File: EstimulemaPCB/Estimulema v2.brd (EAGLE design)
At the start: 151 x 162 mm, 159 parts, among them IC3 74AC14N, IC4 ISO7240S, J1 JUMPERS12MM, J2 J15MM, J3 J_7MM, J4 JUMPERS5MM, J5 JUMPERS7MM, J6 J7MM, K2 HC-06, Q17 TIP48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

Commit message: last version pcb file
ultima version pcb
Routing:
- net GPIO5: track 219.2 -> 222.0 mm
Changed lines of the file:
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@@
 <drawing>
 <settings>
-<setting alwaysvectorfont="yes"/>
+<setting alwaysvectorfont="no"/>
 <setting verticaltext="up"/>
 </settings>
@@
 </layers>
 <board>
-<fusionsync huburn="a.cGVyc29uYWw6dWUyOGM0MjA1" projecturn="a.cGVyc29uYWw6dWUyOGM0MjA1IzIwMTcxMjI2MTA5OTE4NzUx" f3durn="urn:adsk.wipprod:dm.lineage:a3TV6h6ST9ayQOR__9NI6g" pcbguid="653ef68f-6985-4a81-9d55-14a2d5d2a77c" lastpulledtime="" lastsyncedchangeguid="1821962e-2547-75dc-39ca-bfed1a03af76"/>
+<fusionsync huburn="a.cGVyc29uYWw6dWUyOGM0MjA1" projecturn="a.cGVyc29uYWw6dWUyOGM0MjA1IzIwMTcxMjI2MTA5OTE4NzUx" f3durn="urn:adsk.wipprod:dm.lineage:a3TV6h6ST9ayQOR__9NI6g" pcbguid="653ef68f-6985-4a81-9d55-14a2d5d2a77c" lastpulledtime="" lastsyncedchangeguid="752f2832-0191-109f-3336-40c44a7aafc6"/>
 <plain>
 <wire x1="1.016" y1="50" x2="152" y2="50" width="0" layer="20"/>
@@
 <wire x1="55.118" y1="196.596" x2="59.69" y2="196.596" width="0.3556" layer="16"/>
 <via x="59.69" y="196.596" extent="1-16" drill="0.9" diameter="2" shape="square"/>
-<wire x1="59.69" y1="196.596" x2="62.484" y2="196.596" width="0.3556" layer="1"/>
+<wire x1="62.484" y1="196.596" x2="59.69" y2="196.596" width="0.3556" layer="1"/>
 <via x="91.186" y="202.692" extent="1-16" drill="0.9" diameter="2" shape="square"/>
 <wire x1="91.186" y1="202.692" x2="100.584" y2="202.692" width="0.3556" layer="16"/>
@@
 <wire x1="124.5362" y1="90.0938" x2="122.936" y2="91.694" width="0.3556" layer="16"/>
 <wire x1="122.936" y1="106.934" x2="122.936" y2="91.694" width="0.3556" layer="16"/>
-<wire x1="62.484" y1="196.596" x2="68.58" y2="202.692" width="0.3556" layer="1"/>
-<wire x1="68.58" y1="202.692" x2="91.186" y2="202.692" width="0.3556" layer="1"/>
 <wire x1="100.584" y1="202.692" x2="101.092" y2="203.2" width="0.3556" layer="1"/>
 <wire x1="124.968" y1="108.966" x2="122.936" y2="106.934" width="0.3556" layer="16"/>
@@
 <wire x1="101.092" y1="203.2" x2="131.064" y2="203.2" width="0.3556" layer="1"/>
 <wire x1="130.81" y1="127.508" x2="132.588" y2="129.286" width="0.3556" layer="1"/>
+<wire x1="65.024" y1="203.2" x2="63.754" y2="201.93" width="0.3556" layer="1"/>
+<wire x1="63.754" y1="201.93" x2="63.754" y2="197.866" width="0.3556" layer="1"/>
+<wire x1="63.754" y1="197.866" x2="62.484" y2="196.596" width="0.3556" layer="1"/>
+<wire x1="91.186" y1="202.692" x2="90.678" y2="203.2" width="0.3556" layer="1"/>
+<wire x1="90.678" y1="203.2" x2="65.024" y2="203.2" width="0.3556" layer="1"/>
 </signal>
 <signal name="GPIO6" class="2">

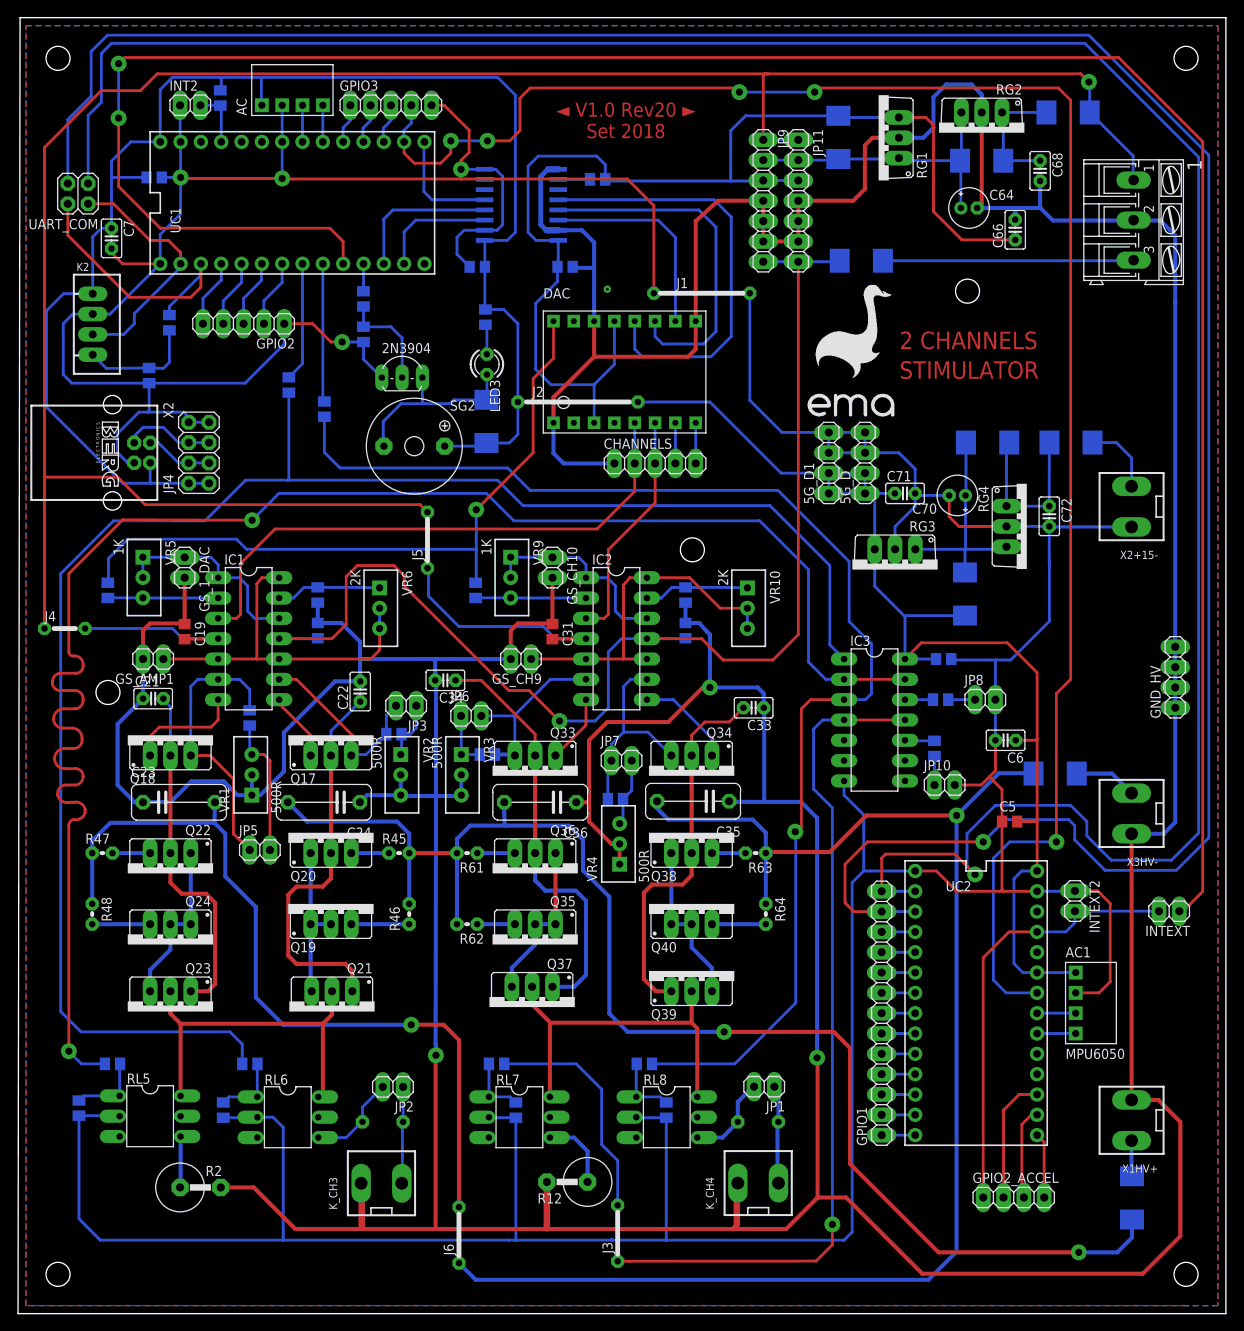
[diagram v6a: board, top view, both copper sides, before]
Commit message: Treinamento y acel
Ahora el stim ino y el diag and train pueden capturar datos del entrenamiento al igual que en el test de exitabilidad
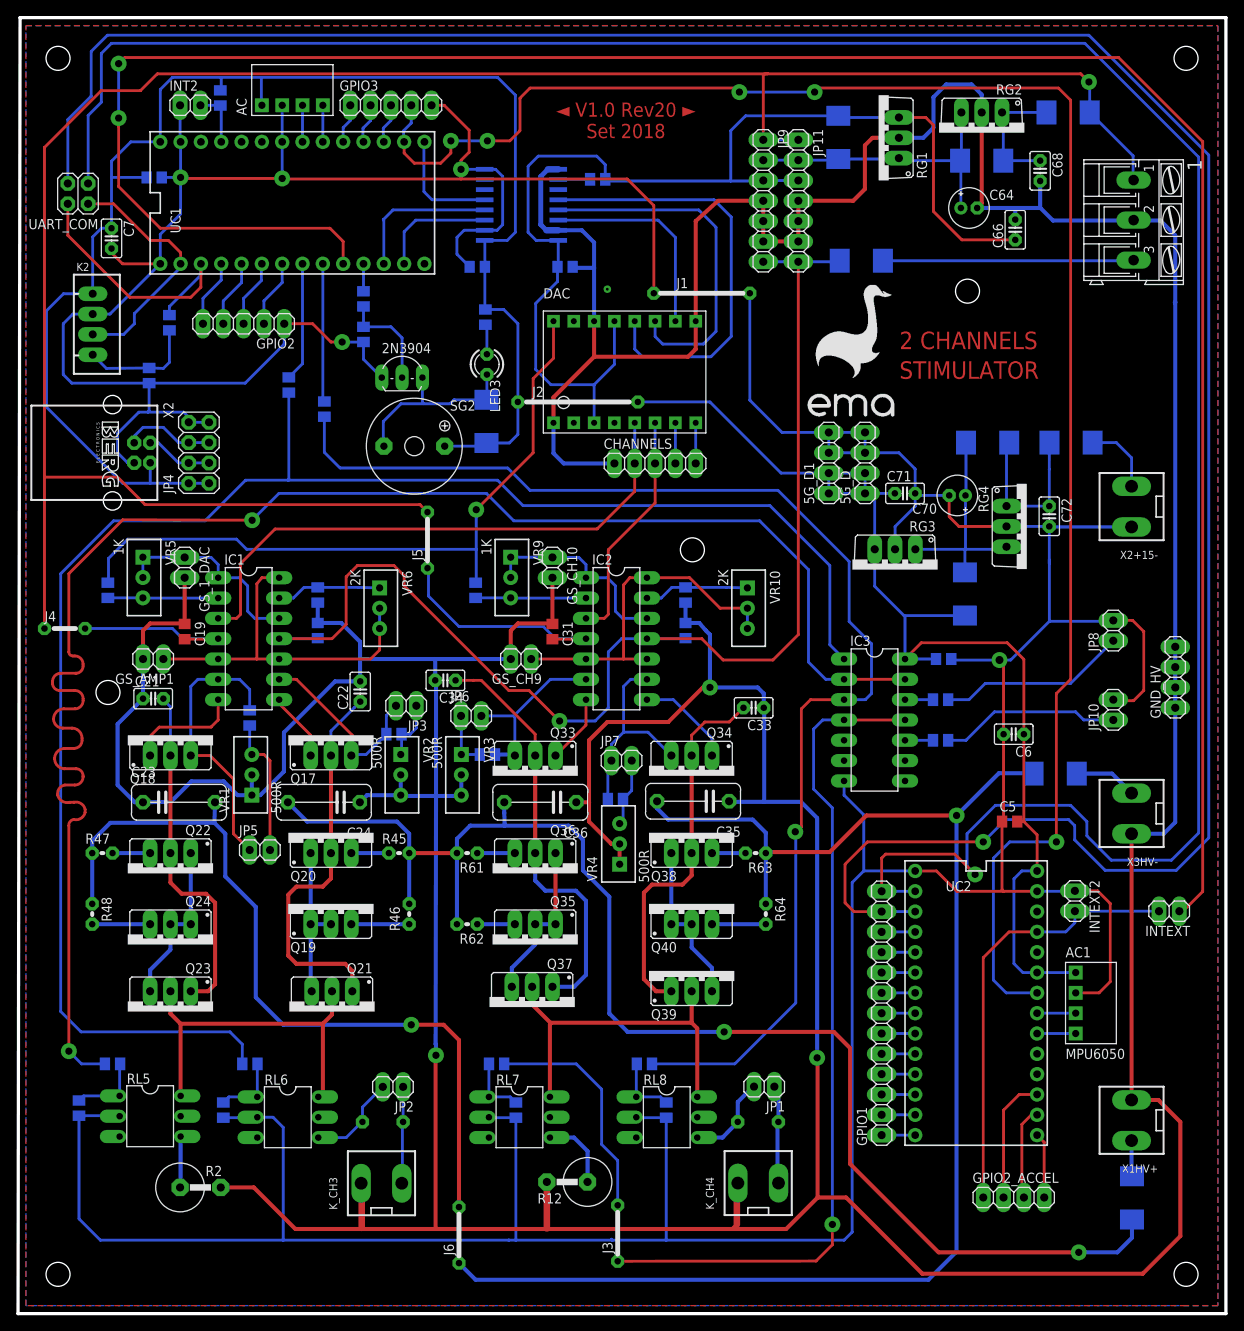
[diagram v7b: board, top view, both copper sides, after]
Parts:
- moved JP10 23.1 mm to (137.9, 125.5), turned to 90 degrees
- moved JP8 18.2 mm to (137.9, 135.4), turned to 90 degrees
- moved C6 1.27 mm to (125.5, 122.4)
- moved R27 1.27 mm to (116.3, 121.7), turned to 180 degrees
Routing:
- net N$32: track 3.37 -> 23.7 mm
- net GND_D: track 669.5 -> 688.8 mm, vias 4 -> 5
- net N$35: track 3.62 -> 22.5 mm
- net +5_D: track 343.0 -> 338.7 mm

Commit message: update pcb y ino para teste calibracion dac
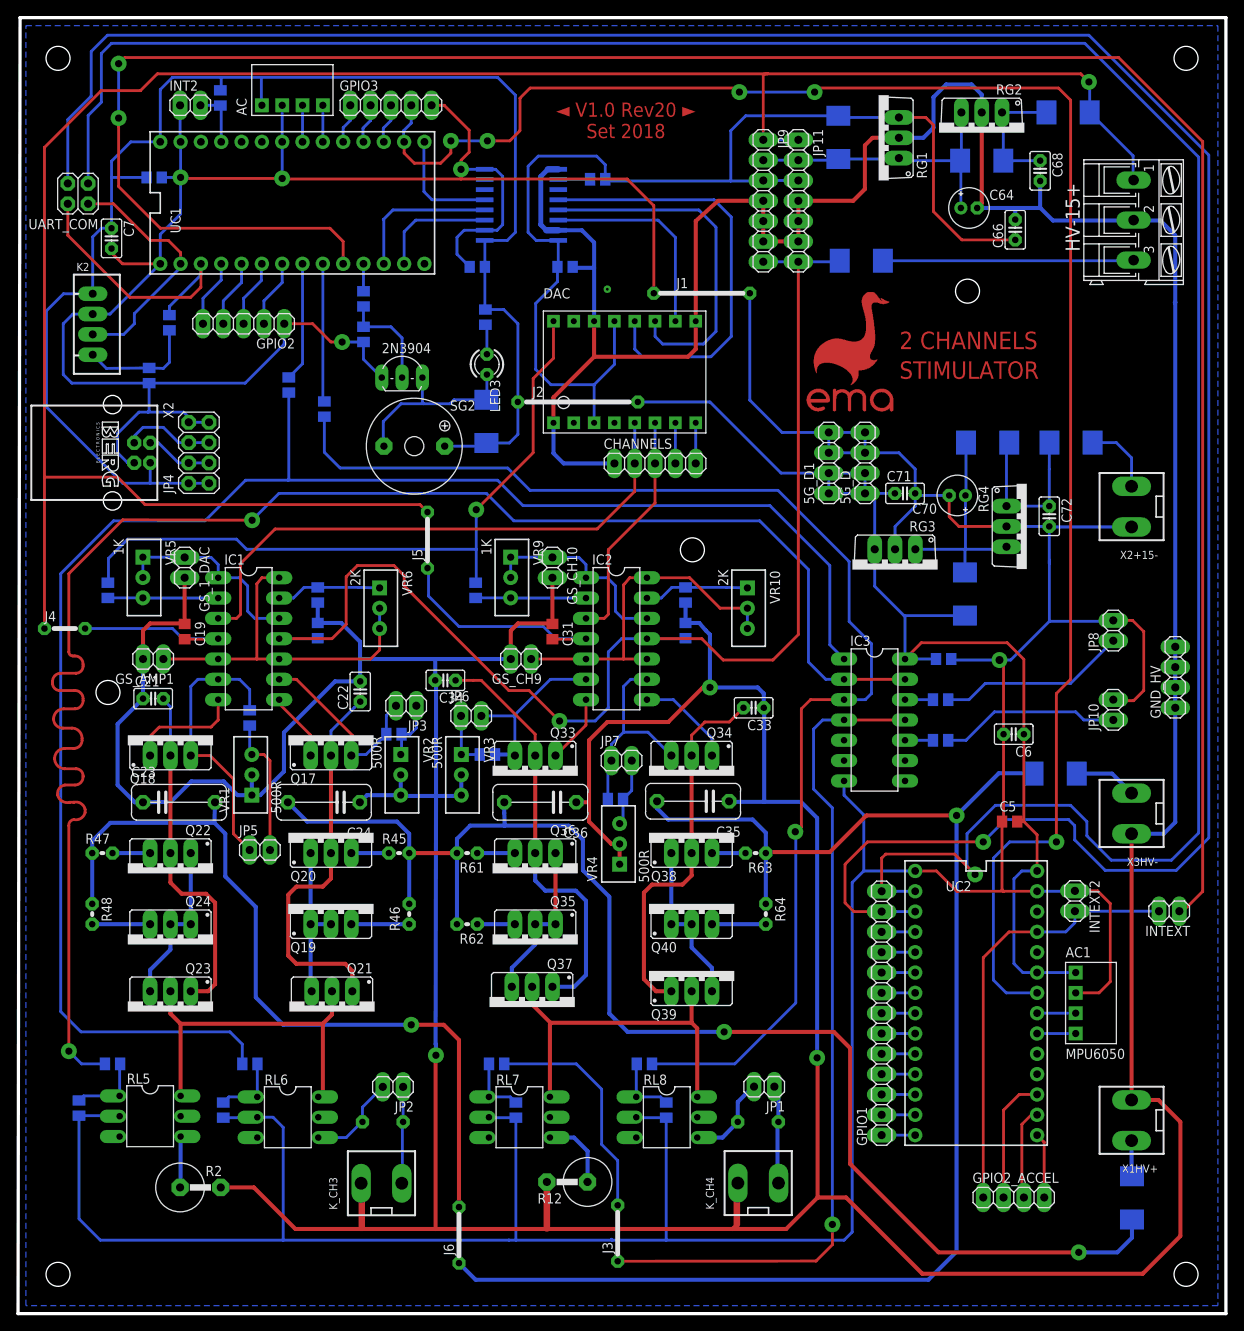
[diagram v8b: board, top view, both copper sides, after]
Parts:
- HV-15+: value PTR500 -> (none)
- R22: value 4K7 -> 470R
- X1HV+, X3HV-: value CONECTOR_5.08 -> (none)
- renumbered 1 to HV-15+
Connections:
- net N$67 renamed RL1
- net N$68 renamed RL2
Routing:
- removed copper zone on layer 1, net GND_HV
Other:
- board text added: "HV+"
